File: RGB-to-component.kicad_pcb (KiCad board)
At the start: 2 copper layers, 50 x 70 mm, 58 parts, among them J1 VGA, J3 USB_C_Receptacle_Power, J4 SCART_CONN, J5 3xRCA_CONN, U1 SC6206B-65K5, U3 RS8752XK, U6 74AHCT1G86, U7 74AHCT1G86, U8 LM1881

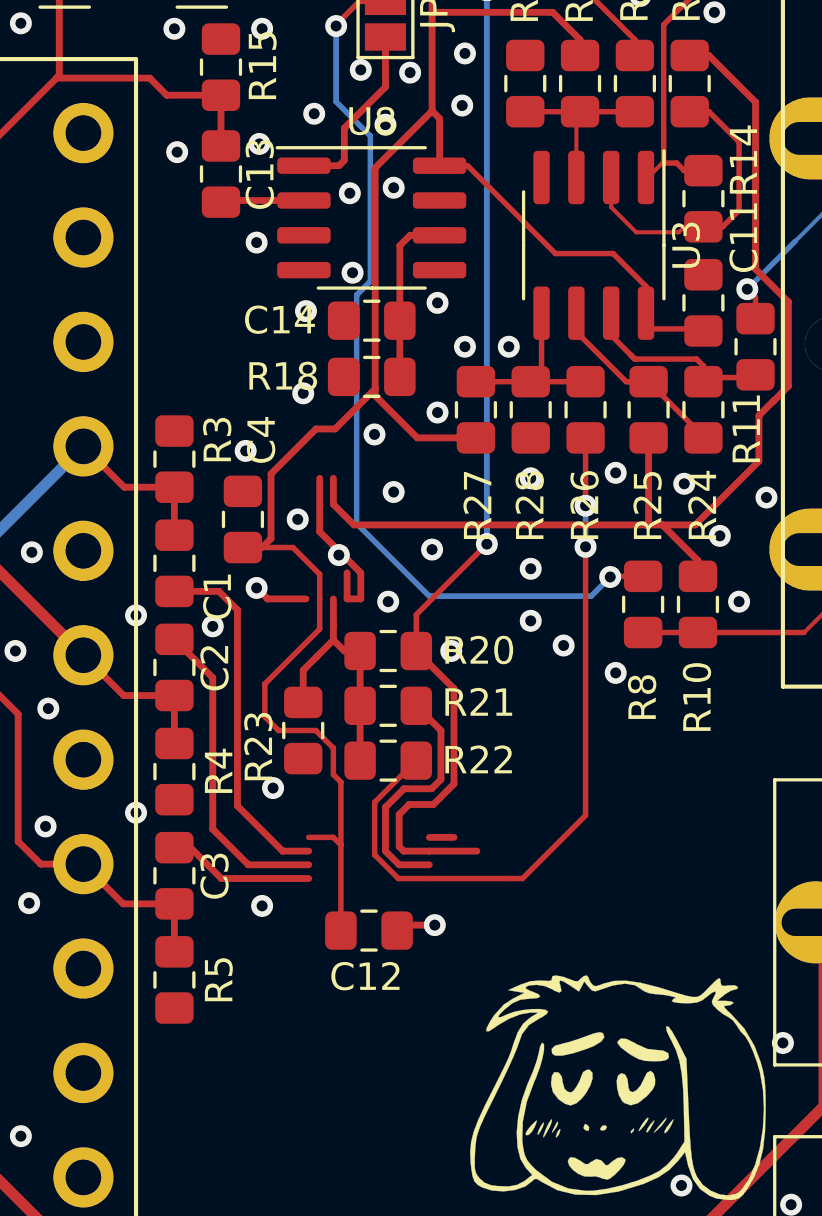
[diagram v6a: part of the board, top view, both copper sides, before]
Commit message: return to THS7374 (temporary single board only)
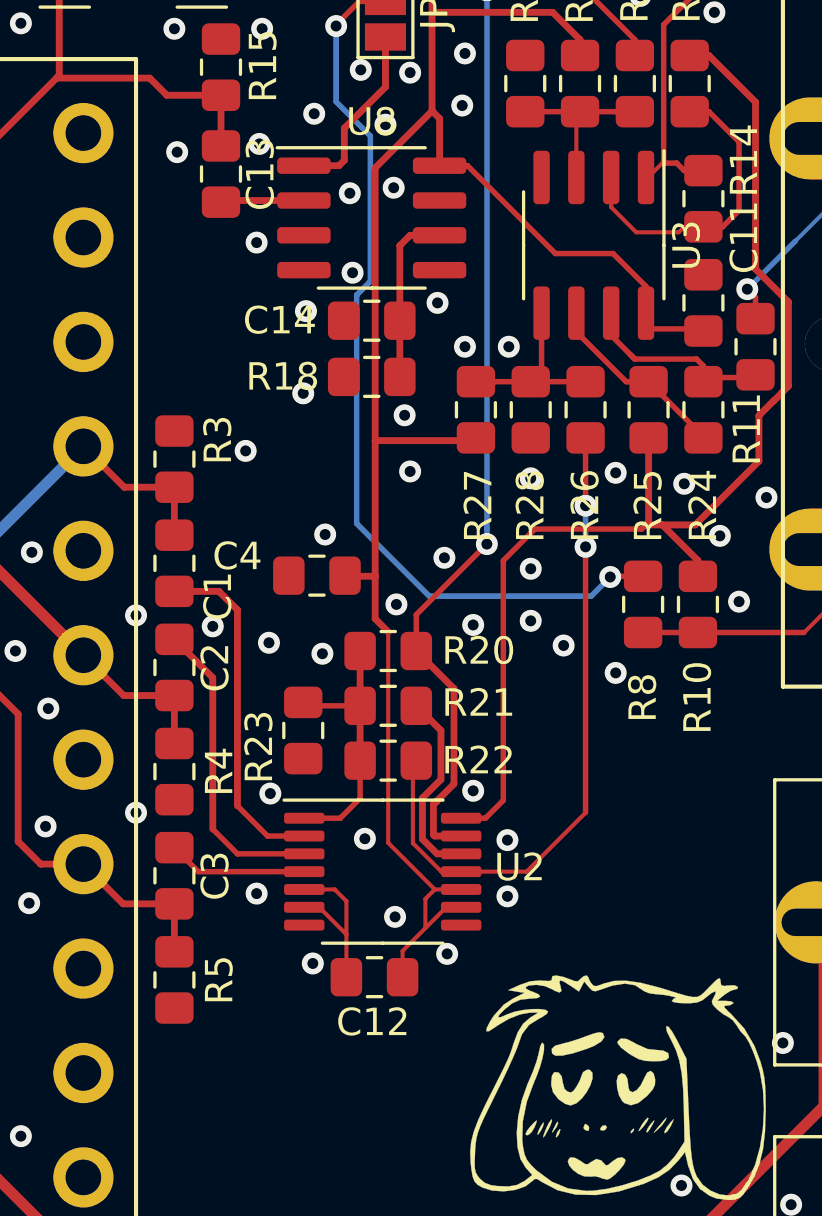
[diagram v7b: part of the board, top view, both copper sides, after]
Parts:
- added U2: THS7374, Package_SO:TSSOP-14_4.4x5mm_P0.65mm, F.Cu at (45.3, 88.8)
- moved C4 3.39 mm to (42.9, 78.0), turned to 180 degrees
- moved C12 1.71 mm to (45.0, 92.6), turned to 180 degrees
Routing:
- net GND: track 10.7 -> 5.89 mm, vias 99 -> 104
- net /2Y: track 40.6 -> 44.4 mm
- net /2R: track 43.8 -> 40.7 mm
- net VCC: track 113.3 -> 110.5 mm
- net /2B: track 26.8 -> 24.4 mm
- net /2G: track 8.91 -> 7.15 mm
- net Net-(C13-Pad2): track 4.18 -> 3.11 mm

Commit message: gerbs update
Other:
- board text added: "RGB to YPbPr 2022-09-09 rev 2.4 wakabavideo.com"
- board text removed: "RGB to YPbPr 2021-05-10 rev 2.4 wakabavideo.com"
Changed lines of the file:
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@@
       (sketchpadsonfab false)
       (subtractmaskfromsilk false)
-      (outputformat 4)
+      (outputformat 1)
       (mirror false)
       (drillshape 0)
       (scaleselection 1)
-      (outputdirectory "./gerbs-single/")
+      (outputdirectory "gerbs-single/")
     )
   )
@@
   (gr_line (start 69.9 110) (end 19.9 110) (layer "Edge.Cuts") (width 0.05))
   (gr_line (start 69.9 40) (end 69.9 110) (layer "Edge.Cuts") (width 0.05))
-  (gr_text "RGB to YPbPr\n2021-05-10 rev 2.4\nwakabavideo.com" (at 58.9 104.9) (layer "F.SilkS")
+  (gr_text "RGB to YPbPr\n2022-09-09 rev 2.4\nwakabavideo.com" (at 58.9 104.9) (layer "F.SilkS")
     (effects (font (size 1.5 1.3) (thickness 0.2)) (justify right))
   )
